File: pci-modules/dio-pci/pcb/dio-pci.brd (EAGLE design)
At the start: 167.6 x 111.2 mm, 111 parts, among them Q1 SSM3J328R, U1 4901, U2 7933, U3 ADN4663, U4 ADN4663, U5 ADN4664, U6 PDS1, U7 4901

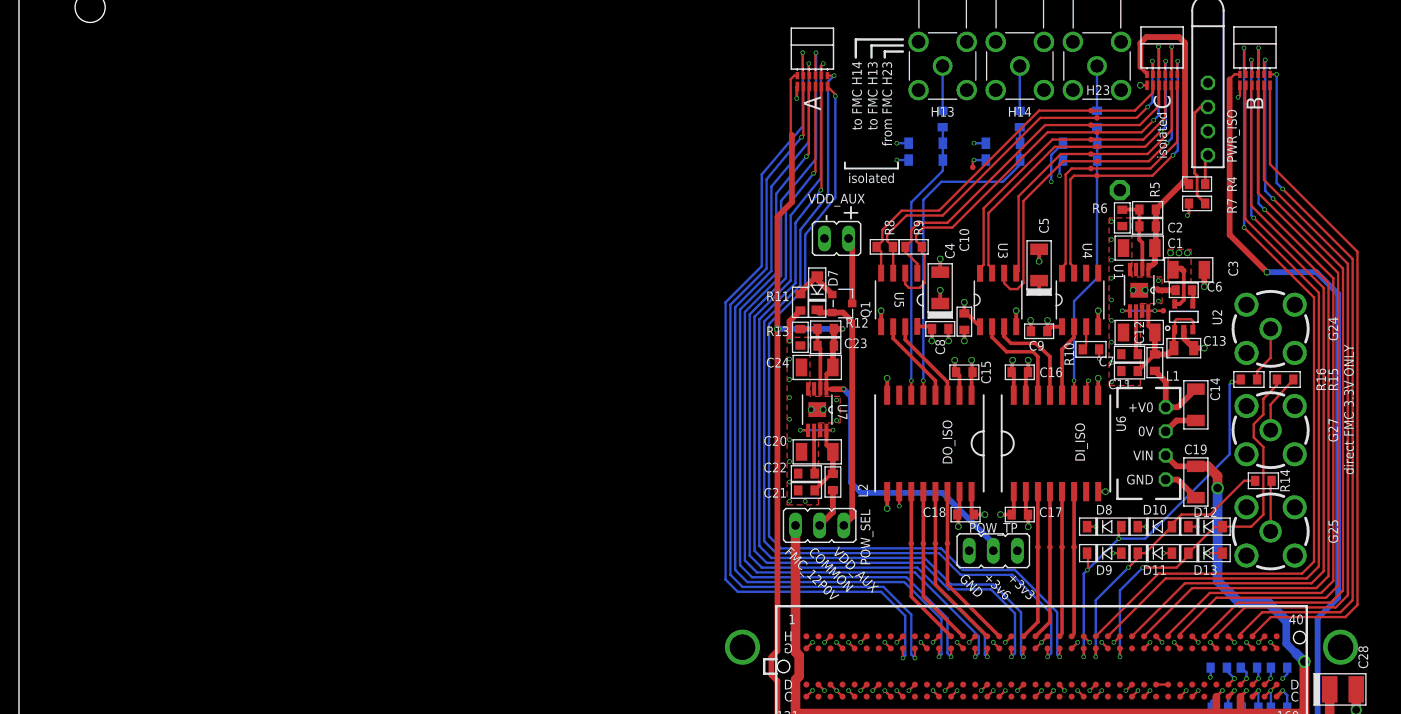
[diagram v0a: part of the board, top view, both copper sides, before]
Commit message: Added some part selections for the pci-dio board.
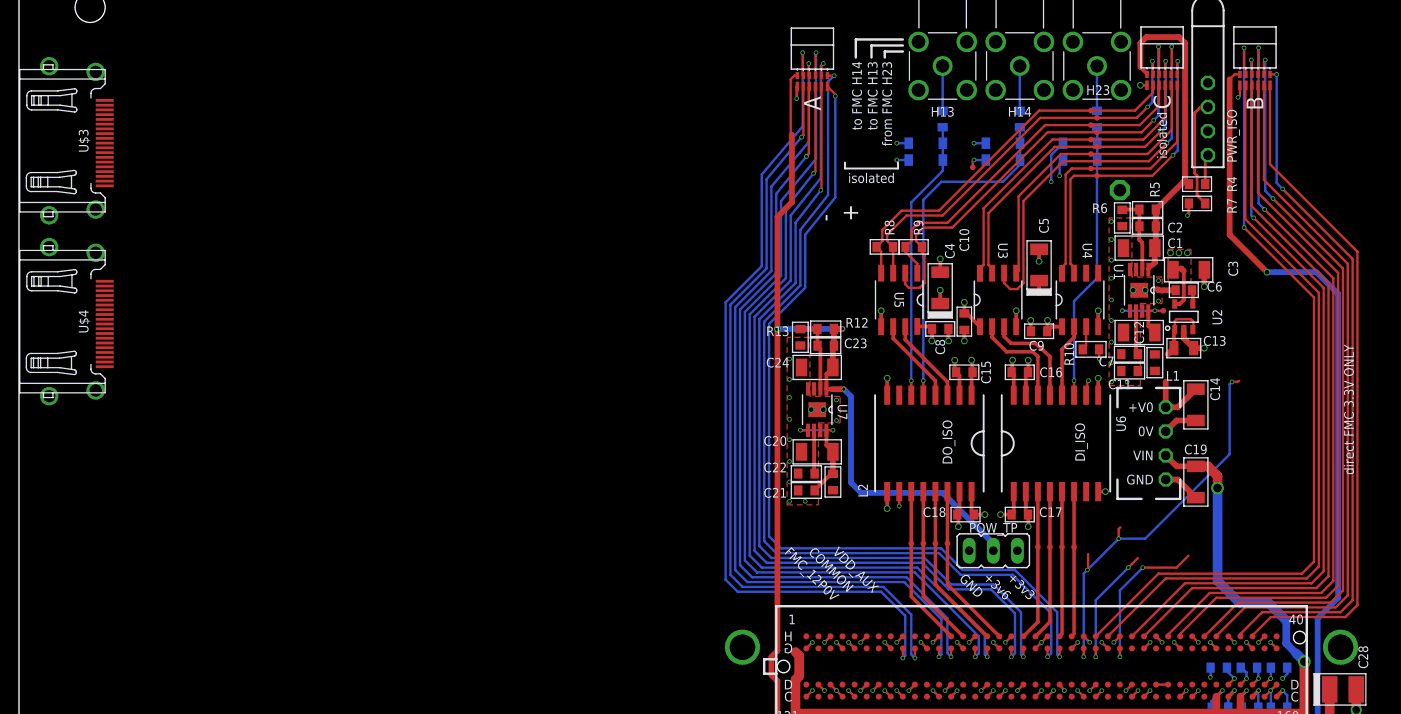
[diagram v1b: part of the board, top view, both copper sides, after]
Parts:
- removed D10, D11, D12, D13, D8, D9: STPS0560Z, jonnew:SOD123
- removed D7: BZT52C7V5, jonnew:SOD123
- removed G24, G25, G27: 142-0701, jonnew:SMA_JACK_142-0701-201
- removed POW_SEL: (no value), jonnew:JP3
- removed Q1: SSM3J328R, jonnew:SOT23-GSD
- removed R11: 10k, jonnew:0603
- removed R14, R15, R16: 100, jonnew:0603
- removed VDD_AUX: (no value), jonnew:JP2
- added U$3, U$4: HDMI, jonnew:HDMI_A
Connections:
- removed net +5V0_ISO-PRE: C14.1, L1.1, U6.P4
- removed net AUX_VDD: L2.1, POW_SEL.2
- removed net N$18: G25.CLK, R14.2
- removed net N$19: G27.CLK, R15.2
- removed net N$2: G24.CLK, R16.2
- removed net N$3: D7.C, POW_SEL.3, Q1.S
- removed net N$6: D7.A, Q1.G, R11.2
- removed net N$7: Q1.D, VDD_AUX.1
- new net N$9: C11.1, C12.1, L1.2, U1.5, U1.8
- net +3V3: no longer D10.C, D12.C, D8.C
- net +3V6: no longer POW_TP.2
- net +5V0: now also C14.1, L1.1, L2.1, U6.P4; no longer C11.1, C12.1, L1.2, U1.5, U1.8
- net 12V_FPGA: no longer POW_SEL.1
- net G24: no longer D8.A, D9.C, R16.1
- net G25: no longer D10.A, D11.C, R14.1
- net G27: no longer D12.A, D13.C, R15.1
- net GND: no longer C20.2, C21.2, C22.2, C24.2, D11.A, D13.A, D9.A, G24.GND$1, G24.GND$2, G24.GND$3, G24.GND$4, G25.GND$1, G25.GND$2, G25.GND$3, G25.GND$4, G27.GND$1, G27.GND$2, G27.GND$3, G27.GND$4, R11.1, R13.2, U7.4, U7.9, VDD_AUX.2
- net GND_ISO: now also C20.2, C21.2, C22.2, C24.2, R13.2, U7.4, U7.9
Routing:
- net N$3: track 26.4 -> 0.00 mm
- net G27: track 42.1 -> 16.6 mm
- net G25: track 30.6 -> 13.1 mm
- net 12V_FPGA: track 129.1 -> 115.7 mm
- net +5V0_ISO-PRE: track 8.27 -> 0.00 mm
- net GND: track 95.0 -> 87.6 mm, vias 84 -> 80
- net N$7: track 7.02 -> 0.00 mm
- net N$19: track 6.25 -> 0.00 mm
- net N$2: track 5.92 -> 0.00 mm
- net N$18: track 5.38 -> 0.00 mm
- net N$6: track 5.34 -> 0.00 mm
- net AUX_VDD: track 4.29 -> 0.00 mm
- net +5V0: track 21.4 -> 18.5 mm
- net +3V3: track 21.3 -> 18.6 mm, vias 10 -> 7
- net N$9: track 0.00 -> 2.54 mm
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
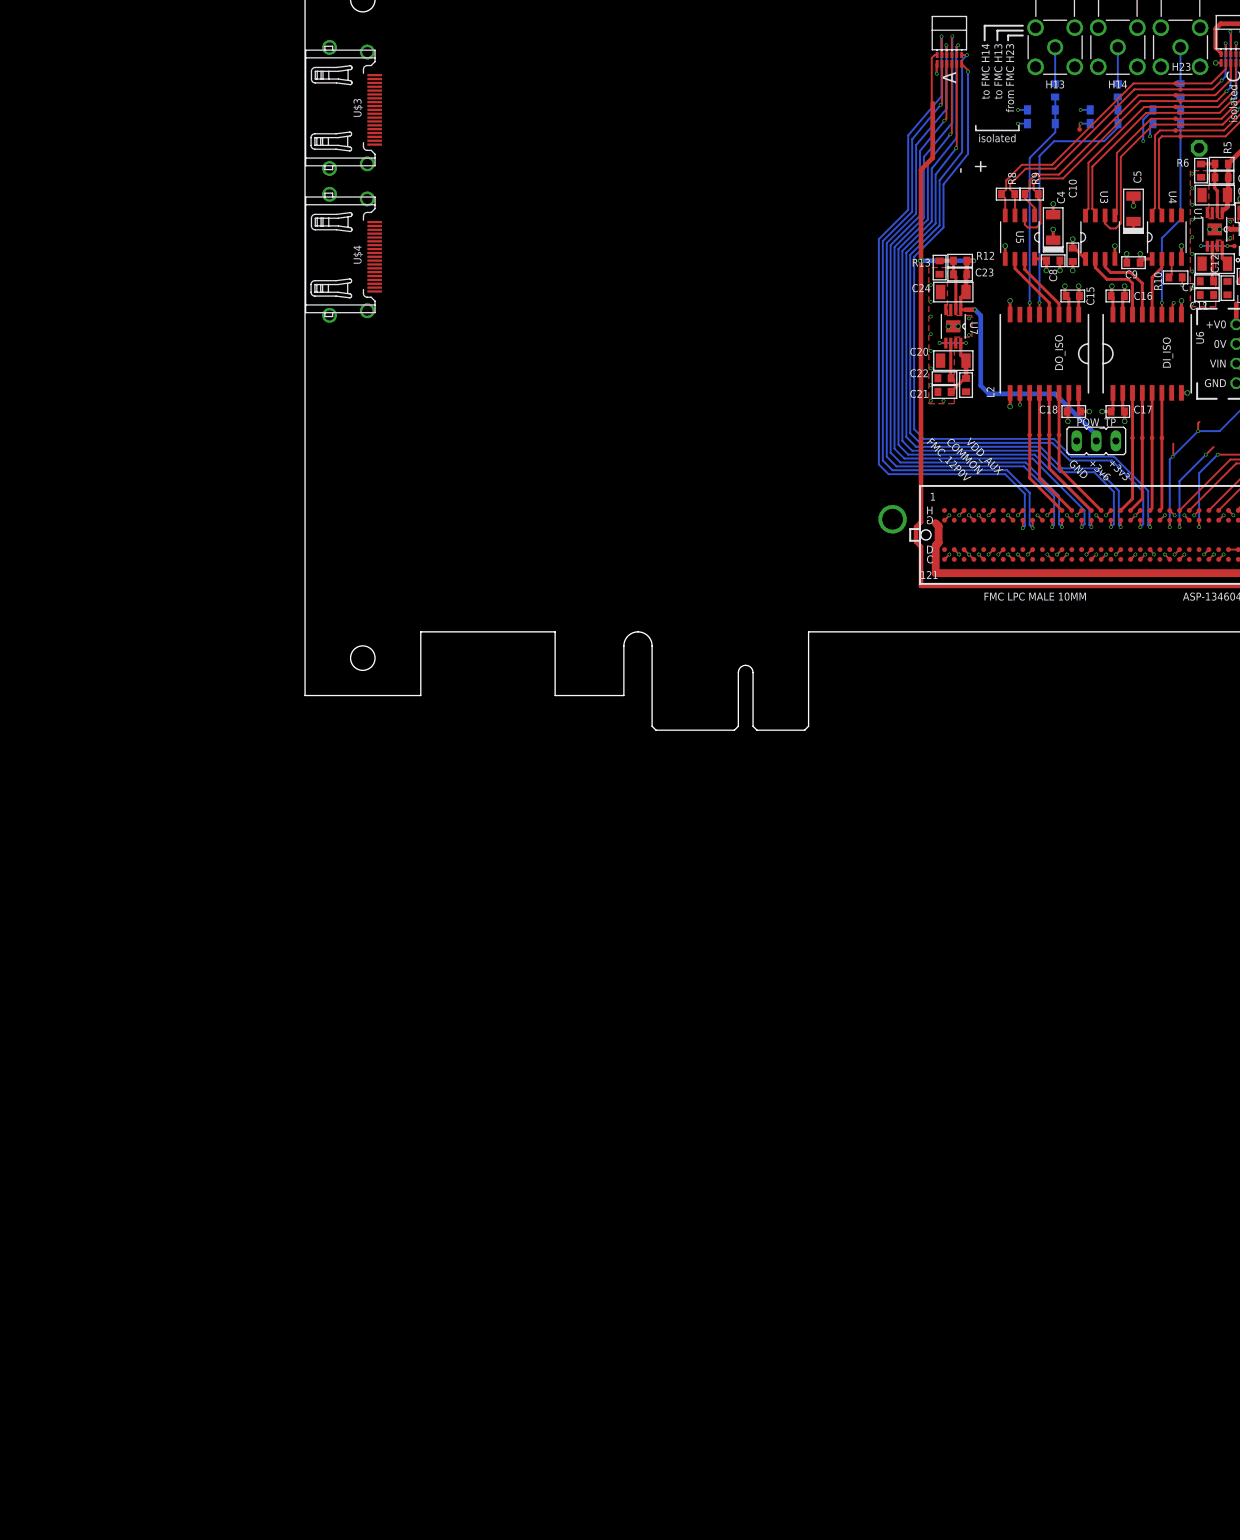
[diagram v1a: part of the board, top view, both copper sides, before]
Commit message: Isolated DIO input circuit design on dio-pic card
- Replace current limit resistors with fast polyfuse with I_trip <
  schottky I_max sustained
- Optional 50 Ohm termination on input SMAs
- TTL Logic-level tolerant line driver on output SMAs
- Programable logic level on input SMAs. Still needs DAC on isolated
  side to set bias voltages
- I really want to replace omnetics with HDMI connectors. Having
  omnetics on a PC chasis seems very wrong because they are made of
  cheese.
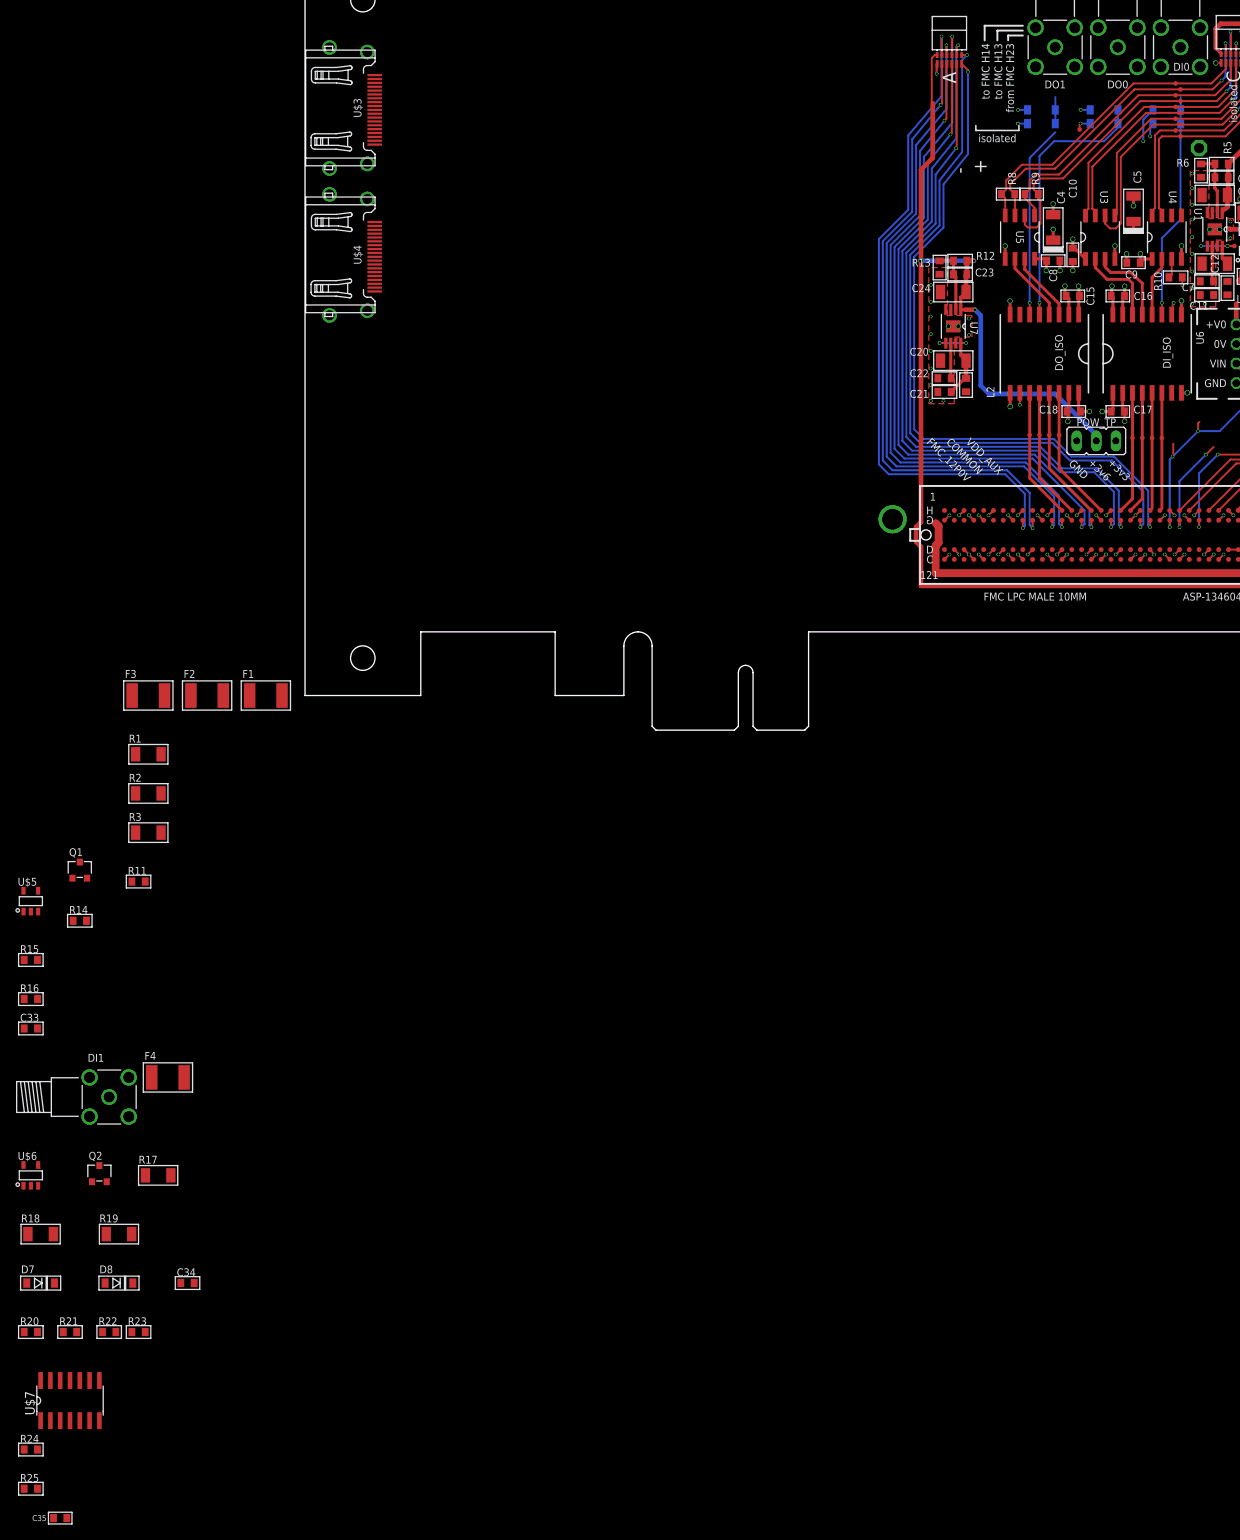
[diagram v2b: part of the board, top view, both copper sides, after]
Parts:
- added C33, C34: 0.1uF, jonnew:0603
- added C35: 0.1uF, RHD2000_eval_board:0603
- added D7, D8: STPS0560Z, jonnew:SOD123
- added DI1: SMA002, jonnew:SMA_JACK_CONREVSMA002-G
- added F1, F2, F3, F4: C014F-2, jonnew:1812
- added Q1, Q2: BSH103, jonnew:SOT23-GSD
- added R11, R14, R20, R21, R24, R25: 2.2k, jonnew:0603
- added R15, R22: 100, jonnew:0603
- added R16, R23: 10k, jonnew:0603
- added R17, R18, R19: 150, 0.25W, jonnew:1206
- added U$5, U$6: ADCMP600, jonnew:SOT-23-5
- added U$7: SN74LVT125, jonnew:SO14
- R1, R2, R3: value 100 -> 150, 0.25W; device jonnew:0603 -> jonnew:1206
- moved R1 159.2 mm to (-20.3, -7.62), flipped to the top, turned to 0 degrees
- moved R2 155.3 mm to (-20.3, -12.7), flipped to the top, turned to 0 degrees
- moved R3 152.0 mm to (-20.3, -17.8), flipped to the top, turned to 0 degrees
- renumbered H13 to DO1, H14 to DO0, H23 to DI0
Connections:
- new net $N1: D7.A, D8.C, F4.2, R17.2, R18.2, R19.2, R20.2, R22.1
- new net $N101: D3.A, D4.C, F1.2, U$7.3, U$7.6
- new net $N102: D5.A, D6.C, F3.2, U$7.11, U$7.8
- new net $N3: D1.A, D2.C, F2.2, R1.2, R11.2, R15.1, R2.2, R3.2
- new net BIAS_DI0: R16.1
- new net BIAS_DI1: R23.1
- new net DI0_TERM_ISO: Q1.G, R14.2
- new net DI1_TERM_ISO: Q2.G, R21.2
- new net N$18: C33.1, R16.2, U$5.4
- new net N$19: R22.2, U$6.3
- new net N$2: Q1.D, R1.1, R2.1, R3.1
- new net N$20: C34.1, R23.2, U$6.4
- new net N$24: R24.1, U$7.1, U$7.4
- new net N$25: R25.1, U$7.10, U$7.13
- new net N$3: R15.2, U$5.3
- new net N$6: DI1.CLK, F4.1
- new net N$7: Q2.D, R17.1, R18.1, R19.1
- new net SOMEWHERE_ISO: U$6.1
- new net V_PROTECT: D1.C, D7.C
- net +3V3_ISO: now also C35.2, R24.2, R25.2, U$5.5, U$6.5, U$7.14; no longer D1.C
- net GND_ISO: now also C33.2, C34.2, C35.1, D8.A, DI1.GND$1, DI1.GND$2, DI1.GND$3, DI1.GND$4, Q1.S, Q2.S, R11.1, R14.1, R20.1, R21.1, U$5.2, U$6.2, U$7.7
- net H13_ISO: now also U$7.12, U$7.9; no longer D5.A, D6.C, R3.1
- net H14_ISO: now also U$7.2, U$7.5; no longer D3.A, D4.C, R2.1
- net H23_ISO: now also U$5.1; no longer D1.A, D2.C, R1.1
- net N$11: now also F2.1; no longer R1.2
- net N$14: now also F1.1; no longer R2.2
- net N$17: now also F3.1; no longer R3.2
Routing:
- net N$17: track 4.72 -> 0.00 mm
- net N$14: track 4.72 -> 0.00 mm
- net N$11: track 4.72 -> 0.00 mm
- net H13_ISO: track 29.6 -> 25.0 mm
- net H14_ISO: track 36.2 -> 32.3 mm
- net H23_ISO: track 29.3 -> 25.8 mm
- net $N3: track 0.00 -> 3.43 mm
- net $N102: track 0.00 -> 3.43 mm
- net $N101: track 0.00 -> 1.81 mm
- net +3V3_ISO: track 33.5 -> 31.7 mm, vias 15 -> 14
- net V_PROTECT: track 0.00 -> 1.80 mm, vias 0 -> 1
